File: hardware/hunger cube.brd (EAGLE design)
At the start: 98.7 x 99 mm, 32 parts, among them IC1 AVR-MEGA8-PPTH, T1 BPX81, T2 BPX81

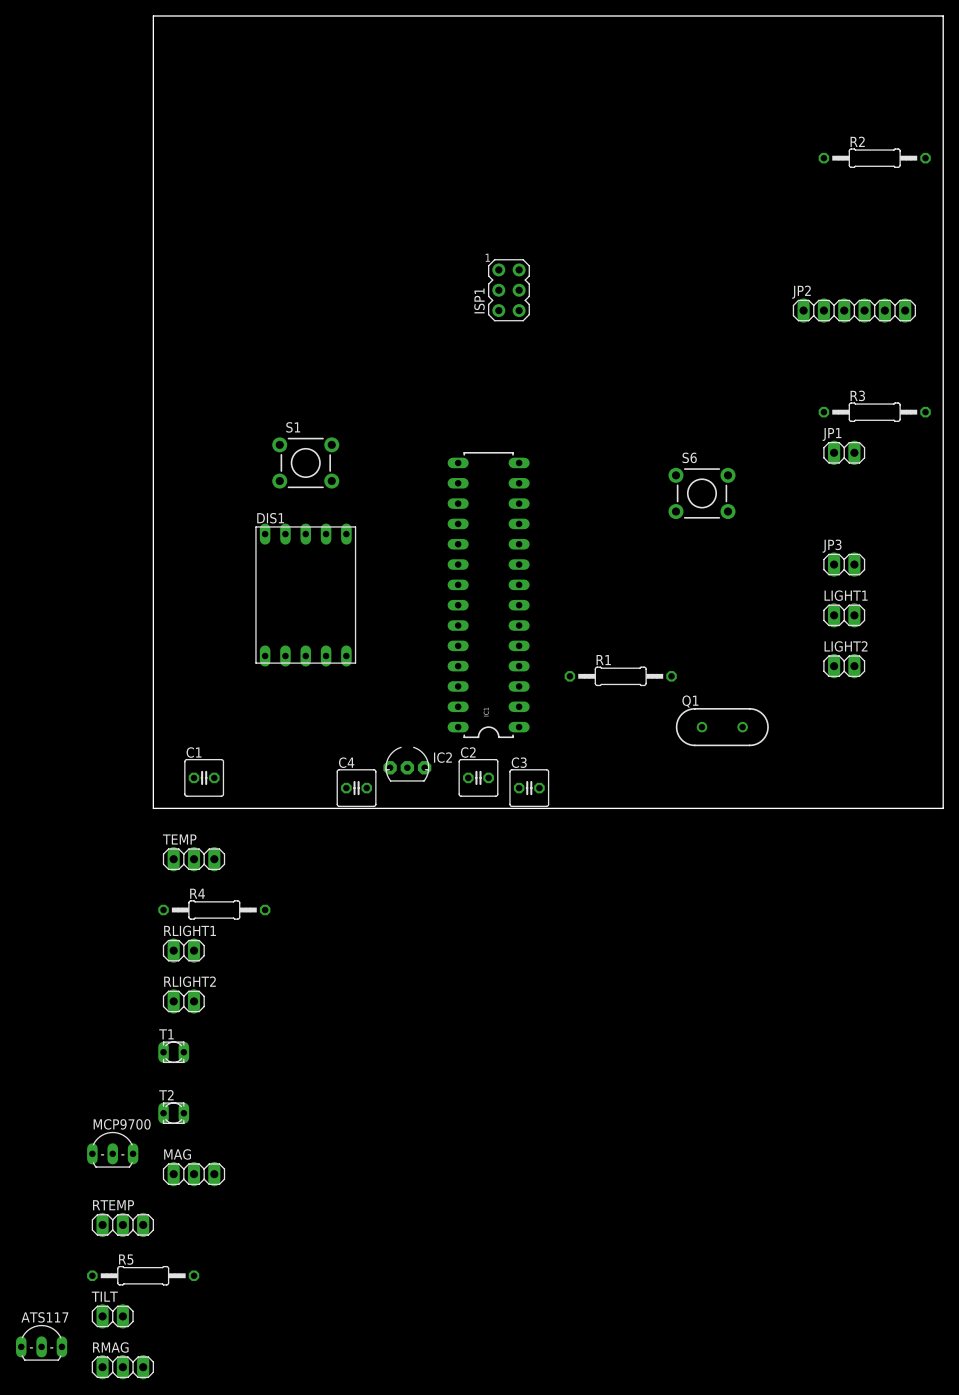
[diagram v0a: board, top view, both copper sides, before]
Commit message: added custom parts for tilt sensor and the secret screw.  Laid out board for the first time.
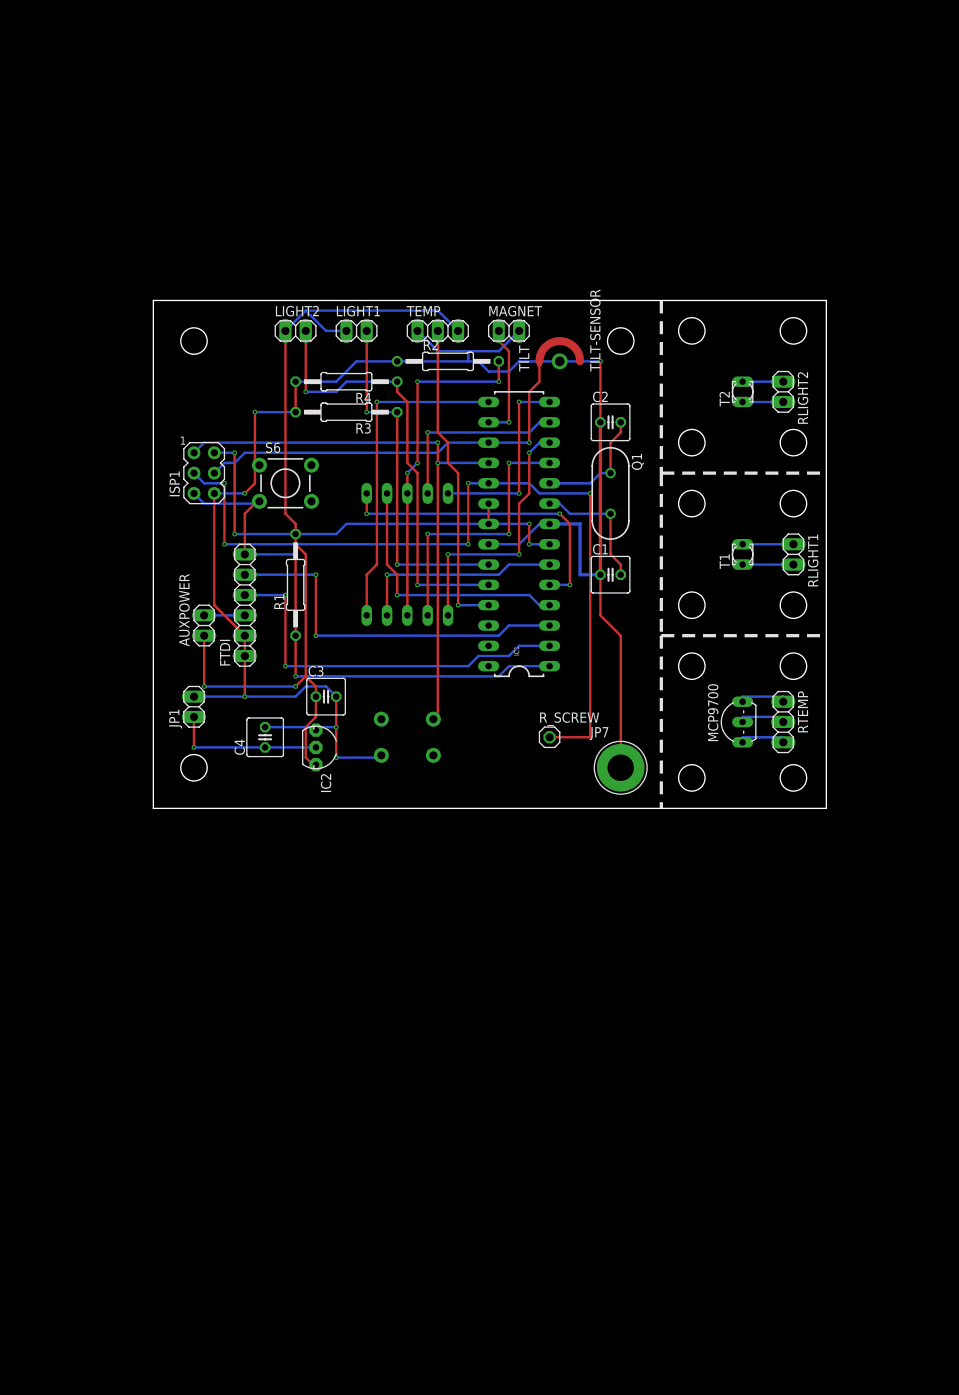
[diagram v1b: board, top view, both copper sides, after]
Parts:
- removed ATS117: (no value), transistor:TO92-EBC
- removed JP2: (no value), pinhead:1X06
- removed JP3: (no value), pinhead:1X02
- removed MAG, RMAG: (no value), pinhead:1X03
- removed R5: 100, resistor:0207/12
- added AUXPOWER, MAGNET: (no value), pinhead:1X02
- added FTDI: (no value), pinhead:1X06
- added JP4, JP5, JP6: STAND-OFF, SparkFun:STAND-OFF
- added JP7: CONNECTED-SCREW-HOLE, connected-screw:SCREW-HOLE-PAD
- added R_SCREW: (no value), pinhead:1X01
- S1: value (none) -> enter
- S6: value (none) -> reset
- TILT: value (none) -> TILT-SENSOR; device pinhead:1X02 -> tilt-sensor:TILT
- moved TILT 131.8 mm to (50.8, 55.9), turned to 90 degrees
- moved T2 114.8 mm to (73.7, 52.1), turned to 90 degrees
- moved RLIGHT2 106.9 mm to (78.7, 52.1), turned to 270 degrees
- moved RTEMP 103.8 mm to (78.7, 10.8), turned to 270 degrees
- moved T1 94.5 mm to (73.7, 31.8), turned to 90 degrees
- moved MCP9700 93.7 mm to (72.4, 10.8), turned to 90 degrees
- moved RLIGHT1 90.9 mm to (80.0, 31.8), turned to 270 degrees
- moved JP1 87.3 mm to (5.08, 12.7), turned to 90 degrees
- moved LIGHT2 80.4 mm to (17.8, 59.7)
- moved TEMP 72.7 mm to (35.6, 59.7)
- moved LIGHT1 70.6 mm to (25.4, 59.7)
- moved R4 68.1 mm to (24.1, 53.3), turned to 180 degrees
- moved R3 66.0 mm to (24.1, 49.5), turned to 180 degrees
- moved R2 59.1 mm to (36.8, 55.9)
- moved C1 56.8 mm to (57.1, 29.2)
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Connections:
- removed net N$23: IC1.18, S1.1
- removed net N$24: IC1.17, TILT.1
- removed net N$25: ATS117.C, RMAG.1
- removed net N$26: ATS117.E, RMAG.3
- removed net N$27: ATS117.B, RMAG.2
- net +5V: now also AUXPOWER.1; no longer JP3.1, MAG.1, R5.2
- net GND: now also FTDI.1, FTDI.2, JP7.SCREW, MAGNET.2, TILT.CENTER; no longer JP2.1, JP2.2, MAG.2, TILT.2
- net MISO: now also IC1.18, S1.1
- net MOSI: now also IC1.17, TILT.SLEEVE
- net N$18: now also MAGNET.1; no longer MAG.3, R5.1
- net N$5: now also AUXPOWER.2, FTDI.3; no longer JP2.3, JP3.2
- net RDX: now also FTDI.4; no longer JP2.4
- net RST: now also FTDI.6; no longer JP2.6
- net SCK: now also IC1.19, R_SCREW.1
- net TDX: now also FTDI.5; no longer JP2.5
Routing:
- net GND: track 0.00 -> 221.9 mm, vias 0 -> 6
- net +5V: track 0.00 -> 164.7 mm, vias 0 -> 6
- net SCK: track 0.00 -> 101.4 mm, vias 0 -> 5
- net MISO: track 0.00 -> 72.3 mm, vias 0 -> 2
- net RST: track 0.00 -> 70.1 mm, vias 0 -> 2
- net N$14: track 0.00 -> 54.9 mm, vias 0 -> 2
- net MOSI: track 0.00 -> 51.6 mm, vias 0 -> 1
- net RDX: track 0.00 -> 48.0 mm, vias 0 -> 2
- net TDX: track 0.00 -> 46.2 mm, vias 0 -> 2
- net LIGHT2: track 0.00 -> 44.4 mm, vias 0 -> 2
- net N$12: track 0.00 -> 42.4 mm, vias 0 -> 4
- net N$11: track 0.00 -> 41.2 mm, vias 0 -> 1
- net N$19: track 0.00 -> 39.2 mm, vias 0 -> 1
- net N$2: track 0.00 -> 38.6 mm, vias 0 -> 3
- net N$7: track 0.00 -> 34.3 mm, vias 0 -> 3
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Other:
- board size 98.7 x 99 mm -> 84.1 x 63.5 mm

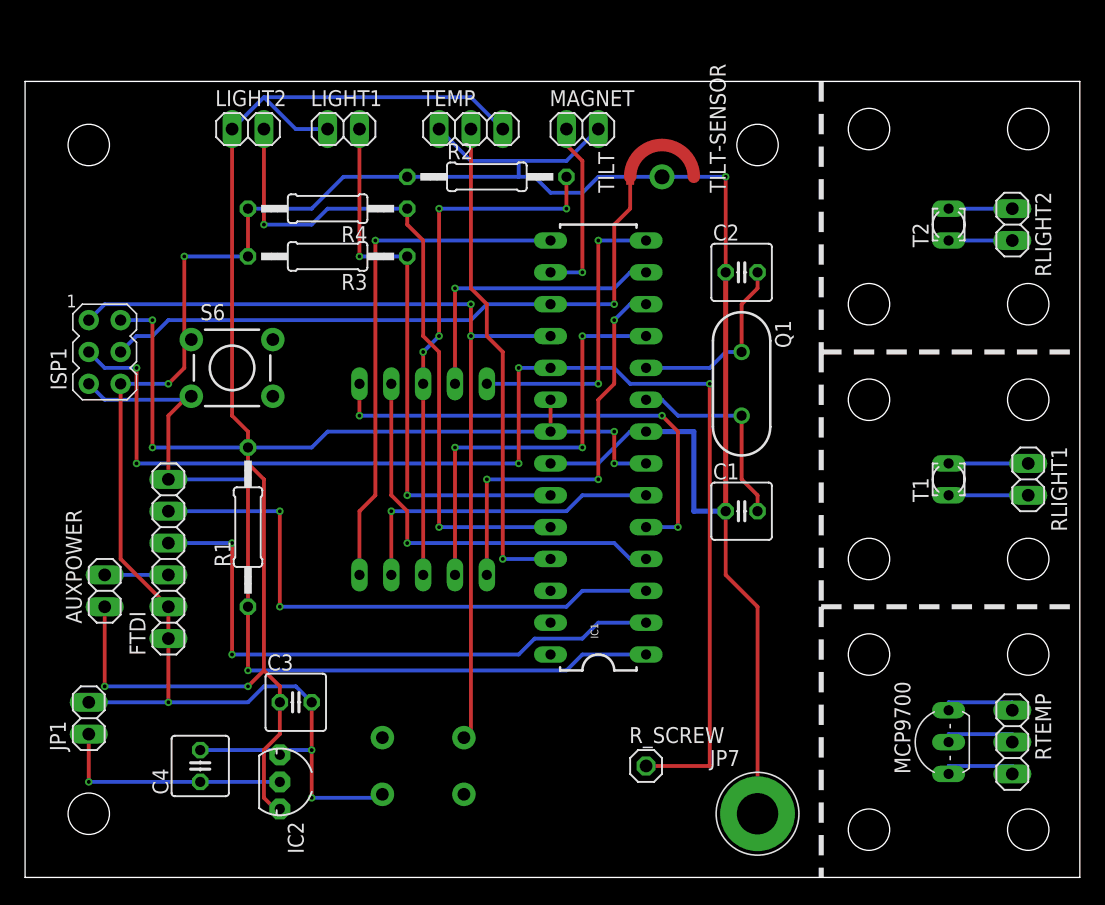
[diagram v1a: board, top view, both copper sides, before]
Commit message: 
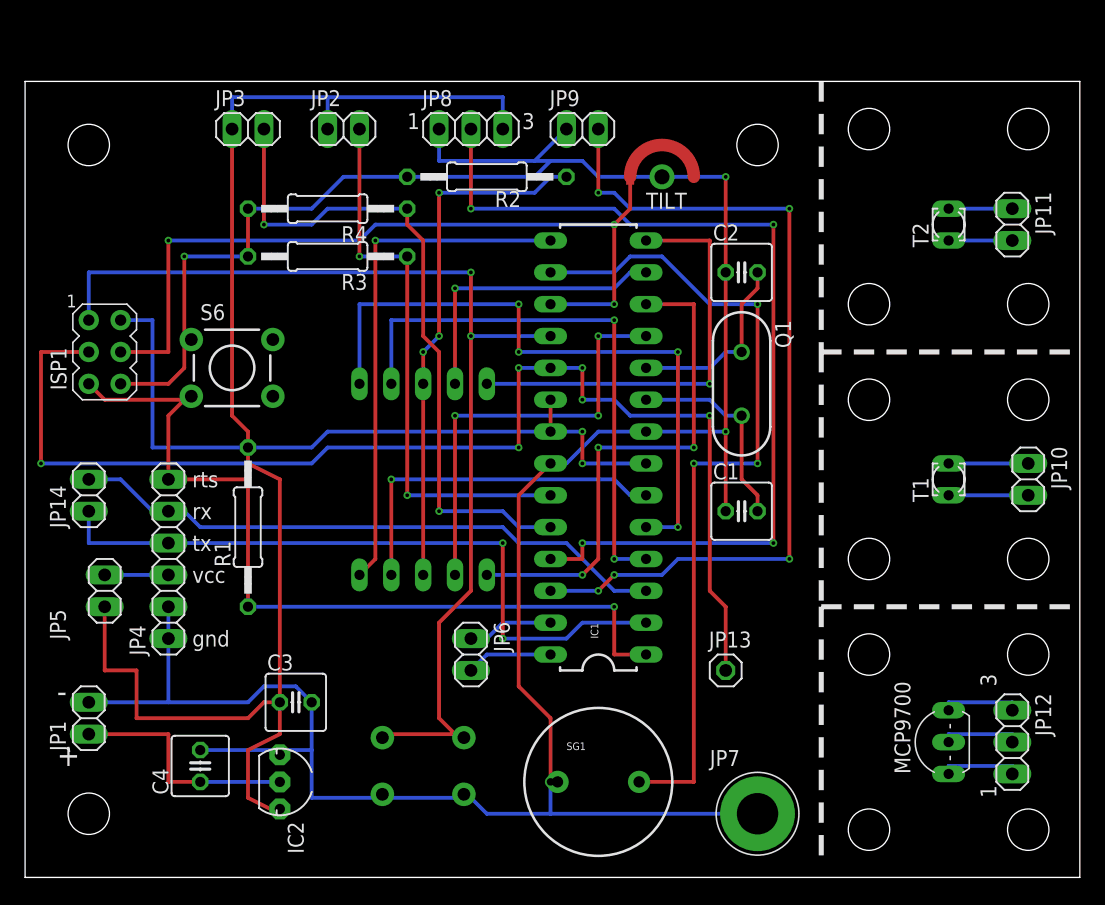
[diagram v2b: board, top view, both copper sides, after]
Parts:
- removed AUXPOWER: (no value), pinhead:1X02
- removed FTDI: (no value), pinhead:1X06
- removed R_SCREW: (no value), pinhead:1X01
- added JP13: R screw, pinhead:1X01
- added JP14: D0-D1, pinhead:1X02
- added SG1: BUZZERPTH, SparkFun:BUZZER-12MM
- added ST1, ST2, ST3: STAND-OFF, SparkFun:STAND-OFF
- JP10: value (none) -> R Light 1
- JP11: value (none) -> R light 2
- JP12: value (none) -> R temp
- JP2: value (none) -> Light1
- JP3: value (none) -> Light 2
- JP4: value STAND-OFF -> FTDI; device SparkFun:STAND-OFF -> pinhead:1X06
- JP5: value STAND-OFF -> Aux Pwr; device SparkFun:STAND-OFF -> pinhead:1X02
- JP6: value STAND-OFF -> A4-A5; device SparkFun:STAND-OFF -> pinhead:1X02
- JP7: value CONNECTED-SCREW-HOLE -> Connected screw hole
- JP8: value (none) -> TEMP
- JP9: value (none) -> Magnet
- moved JP5 63.1 mm to (6.35, 22.9), turned to 90 degrees
- moved JP4 33.6 mm to (11.4, 25.4), turned to 90 degrees
- moved JP6 33.0 mm to (35.6, 17.8), turned to 270 degrees
- renumbered LIGHT1 to JP2, LIGHT2 to JP3, MAGNET to JP9, RLIGHT1 to JP10, RLIGHT2 to JP11, RTEMP to JP12, TEMP to JP8
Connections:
- new net N$23: IC1.16, SG1.+
- new net N$24: IC1.27, JP6.1
- new net N$25: IC1.28, JP6.2
- net +5V: now also JP5.1; no longer AUXPOWER.1
- net GND: now also JP4.1, JP4.2, JP9.1, S1.3, SG1.-; no longer FTDI.1, FTDI.2, JP9.2
- net MISO: now also S1.2
- net N$18: now also IC1.26, JP9.2; no longer IC1.16, JP9.1
- net N$5: now also JP4.3, JP5.2; no longer AUXPOWER.2, FTDI.3
- net RDX: now also JP14.1, JP4.4; no longer FTDI.4
- net RST: now also JP4.6; no longer FTDI.6
- net SCK: now also JP13.1; no longer R_SCREW.1
- net TDX: now also JP14.2, JP4.5; no longer FTDI.5
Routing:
- net N$23: track 0.00 -> 66.2 mm, vias 0 -> 3
- net N$18: track 14.5 -> 68.9 mm, vias 1 -> 5
- net N$19: track 39.2 -> 75.5 mm, vias 1 -> 4
- net MISO: track 72.3 -> 86.4 mm
- net N$2: track 38.6 -> 52.1 mm, vias 3 -> 4
- net MOSI: track 51.6 -> 64.6 mm, vias 1 -> 3
- net N$1: track 32.8 -> 44.5 mm, vias 1 -> 2
- net N$10: track 24.1 -> 34.3 mm, vias 2 -> 1
- net GND: track 221.9 -> 231.8 mm, vias 6 -> 4
- net N$8: track 32.8 -> 41.2 mm
- net RDX: track 48.0 -> 55.1 mm
- net N$25: track 0.00 -> 6.88 mm
- net N$24: track 0.00 -> 6.88 mm
- net +5V: track 164.7 -> 170.5 mm, vias 6 -> 2
- net SCK: track 101.4 -> 96.8 mm, vias 5 -> 6
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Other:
- board text added: "+"
- board text added: "-"
- board text added: "1"
- board text added: "3"
- board text added: "gnd"
- board text added: "rts"
- board text added: "rx"
- board text added: "tx"
- board text added: "vcc"

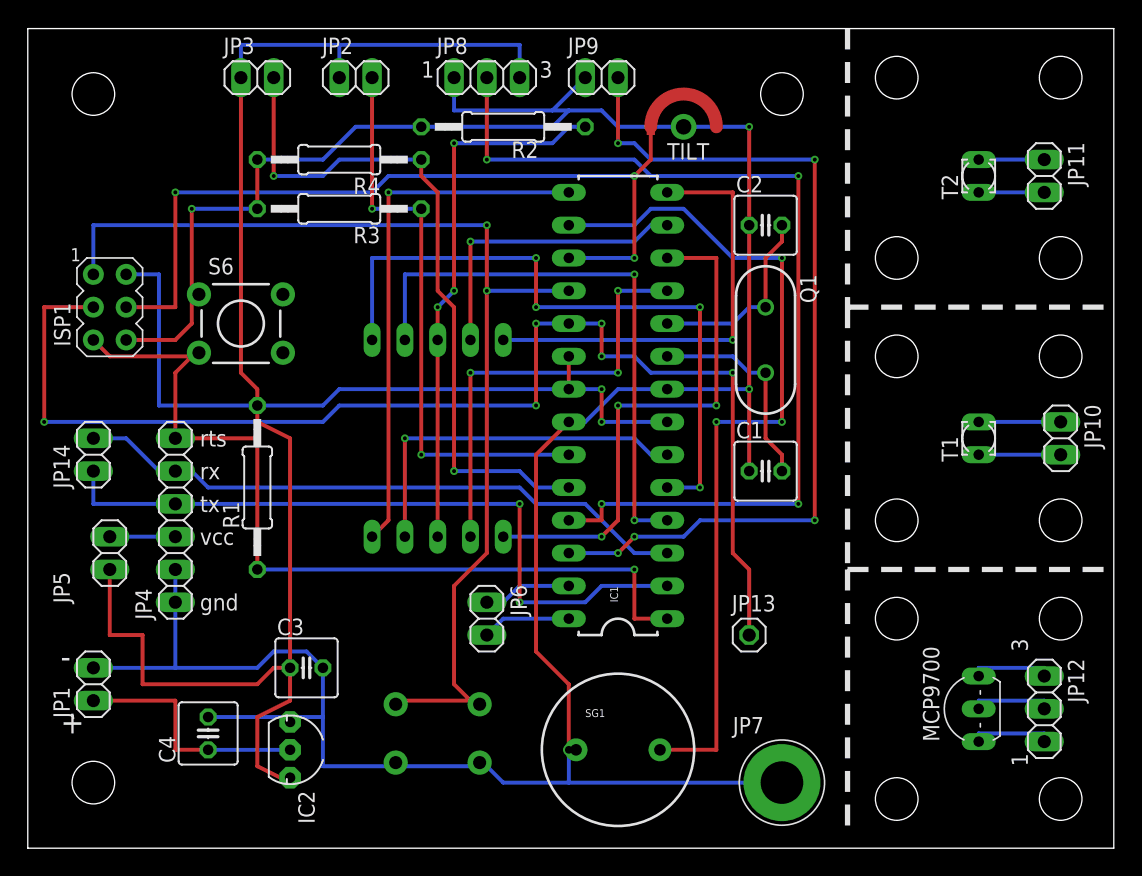
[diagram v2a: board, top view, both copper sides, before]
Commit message: Added box svg to archive, measured dimentions of parts of board for box, and tweaked where some holes are.
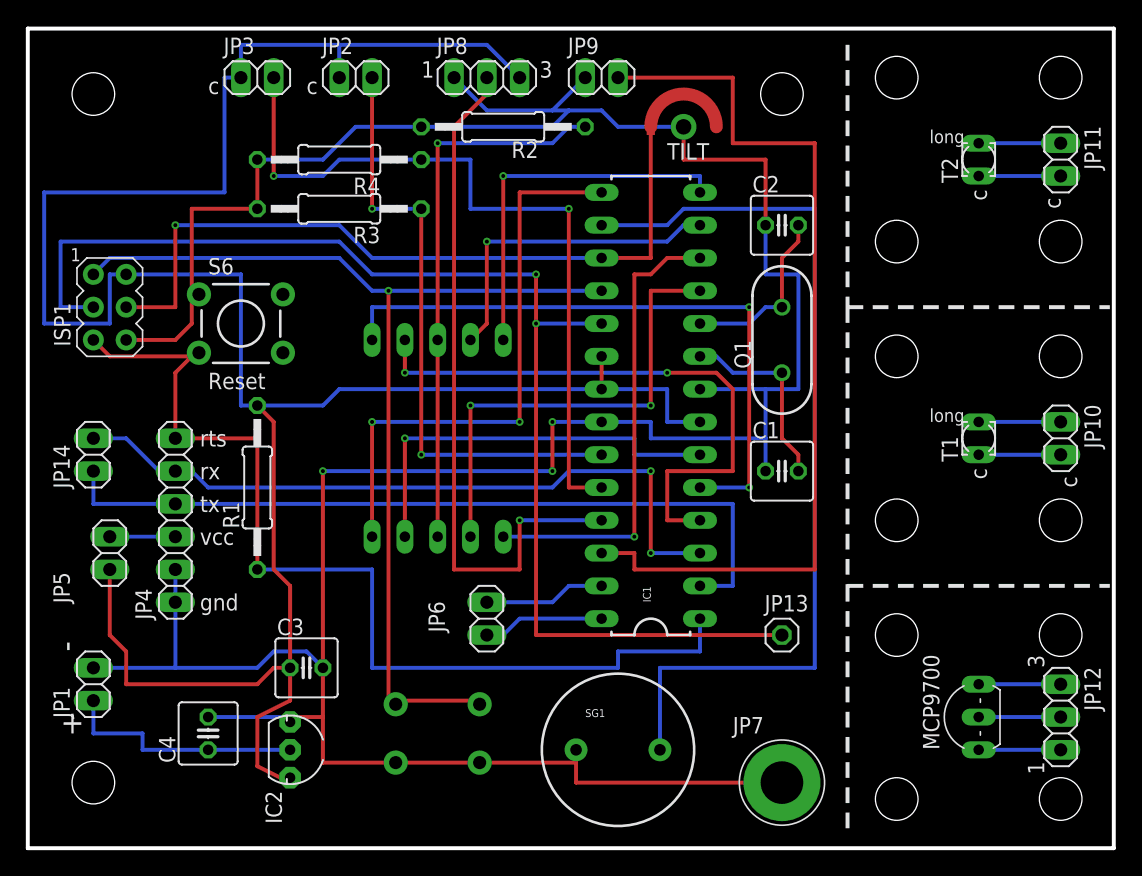
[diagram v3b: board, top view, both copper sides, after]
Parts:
- C1, C2: value (none) -> 18pF
- IC2: value (none) -> LDO 5v
- JP14: value D0-D1 -> D0 D1
- JP6: value A4-A5 -> A5 A4
- MCP9700: value (none) -> temp
- Q1: value (none) -> 16Mhz
- T1, T2: value BPX81 -> PT204
- moved IC1 2.54 mm to (48.3, 34.3)
- moved JP13 2.54 mm to (58.4, 16.5)
- moved JP11 1.80 mm to (80.0, 53.3)
- moved JP12 1.42 mm to (80.0, 10.2)
- moved C1 1.27 mm to (58.4, 29.2)
- moved C2 1.27 mm to (58.4, 48.3)
- moved Q1 1.27 mm to (58.4, 39.4)
- moved T2 1.27 mm to (73.7, 53.3)
- moved MCP9700 0.63 mm to (72.4, 10.2)
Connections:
- net LIGHT2 renamed A0-LIGHT1
- net MISO renamed D12-MISO-ENTER
- net MOSI renamed D11-MOSI-TILT
- net N$1 renamed D2-SEGA
- net N$10 renamed D8-SEGG
- net N$11 renamed D9-DP
- net N$14 renamed A1-LIGHT2
- net N$18 renamed A3-MAGNET
- net N$19 renamed A2-TEMP
- net N$2 renamed D3-SEBB
- net N$23 renamed D10-BUZZER
- net N$24 renamed A4
- net N$25 renamed A5
- net N$6 renamed D4-SEGC
- net N$7 renamed D5-SEGD
- net N$8 renamed D6-SEGE
- net N$9 renamed D7-SEGF
- net RDX renamed D0-RDX
- net SCK renamed D13-SCK-SCREW
- net TDX renamed D1-TDX
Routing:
- net GND: track 231.8 -> 253.0 mm, vias 4 -> 3
- net A2-TEMP: track 75.5 -> 54.4 mm, vias 4 -> 1
- net +5V: track 170.5 -> 188.8 mm, vias 2 -> 0
- net RST: track 68.3 -> 78.5 mm, vias 1 -> 0
- net D1-TDX: track 48.1 -> 55.4 mm, vias 0 -> 2
- net D12-MISO-ENTER: track 86.4 -> 79.9 mm, vias 2 -> 1
- net D11-MOSI-TILT: track 64.6 -> 58.2 mm, vias 3 -> 1
- net D0-RDX: track 55.1 -> 61.0 mm, vias 2 -> 0
- net D6-SEGE: track 41.2 -> 36.1 mm, vias 3 -> 1
- net D8-SEGG: track 34.3 -> 29.2 mm
- net A1-LIGHT2: track 54.2 -> 58.9 mm
- net D10-BUZZER: track 66.2 -> 70.9 mm, vias 3 -> 0
- net D9-DP: track 41.2 -> 44.4 mm, vias 1 -> 2
- net D4-SEGC: track 28.5 -> 31.8 mm
- net A4: track 6.88 -> 9.42 mm
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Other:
- board text added: "Reset"
- board text added: "c"
- board text added: "enter"
- board text added: "long"
